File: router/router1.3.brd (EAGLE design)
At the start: 72.1 x 38.4 mm, 20 parts, among them IC1 REG1117, J1 nRF24, J4 6_PIN_SERIAL_CABLEPTH

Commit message: New router 1.3
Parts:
- S3: value FLASH -> USER
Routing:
- net GND: track 71.8 -> 69.4 mm
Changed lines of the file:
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@@
 </element>
 <element name="J4" library="SparkFun-Connectors" package="FTDI_BASIC" value="6_PIN_SERIAL_CABLEPTH" x="49.2125" y="-22.225" rot="MR0"/>
-<element name="S3" library="SparkFun-Switches" package="TACTILE_SWITCH_PTH_6.0MM" value="FLASH" x="-10.795" y="-16.8275" rot="MR270">
+<element name="S3" library="SparkFun-Switches" package="TACTILE_SWITCH_PTH_6.0MM" value="USER" x="-10.795" y="-16.8275" rot="MR270">
 <attribute name="PROD_ID" value=" SWCH-08441" x="-10.795" y="-16.8275" size="1.778" layer="28" rot="MR270" display="off"/>
 <attribute name="SF_SKU" value="COM-00097" x="-10.795" y="-16.8275" size="1.778" layer="28" rot="MR270" display="off"/>
@@
 <contactref element="C3" pad="2"/>
 <contactref element="S2" pad="3"/>
-<contactref element="S1" pad="3"/>
 <contactref element="C4" pad="2"/>
 <contactref element="C5" pad="2"/>
@@
 </polygon>
 <contactref element="J4" pad="GND"/>
-<contactref element="S3" pad="3"/>
 <contactref element="IC1" pad="1"/>
 <contactref element="J2" pad="8"/>
@@
 <wire x1="21.6281" y1="-11.1055875" x2="21.6281" y2="-3.8354" width="0.1524" layer="1"/>
 <wire x1="35.8775" y1="7.115" x2="41.5925" y2="7.115" width="0.1524" layer="1"/>
-<wire x1="-8.5344" y1="5.1562" x2="-8.5344" y2="7.59323125" width="0.1524" layer="16"/>
 <wire x1="-7.7216" y1="10.0584" x2="-6.35" y2="11.43" width="0.1524" layer="16"/>
 <wire x1="-8.5344" y1="7.59323125" x2="-7.7216" y2="8.40603125" width="0.1524" layer="16"/>
@@
 <wire x1="26.67" y1="6.0325" x2="26.67" y2="5.715" width="0.1524" layer="1"/>
 <wire x1="25.5875" y1="7.115" x2="26.67" y2="6.0325" width="0.1524" layer="1"/>
+<contactref element="S1" pad="3"/>
+<contactref element="S3" pad="3"/>
+<wire x1="-8.5344" y1="-4.0513" x2="-8.5344" y2="-13.5763" width="0" layer="19" extent="1-1"/>
+<wire x1="-8.5344" y1="5.1562" x2="-8.5344" y2="-4.0513" width="0" layer="19" extent="1-1"/>
+<wire x1="-8.5344" y1="7.59323125" x2="-8.5344" y2="5.1562" width="0" layer="19" extent="16-16"/>
 </signal>
 <signal name="RST">

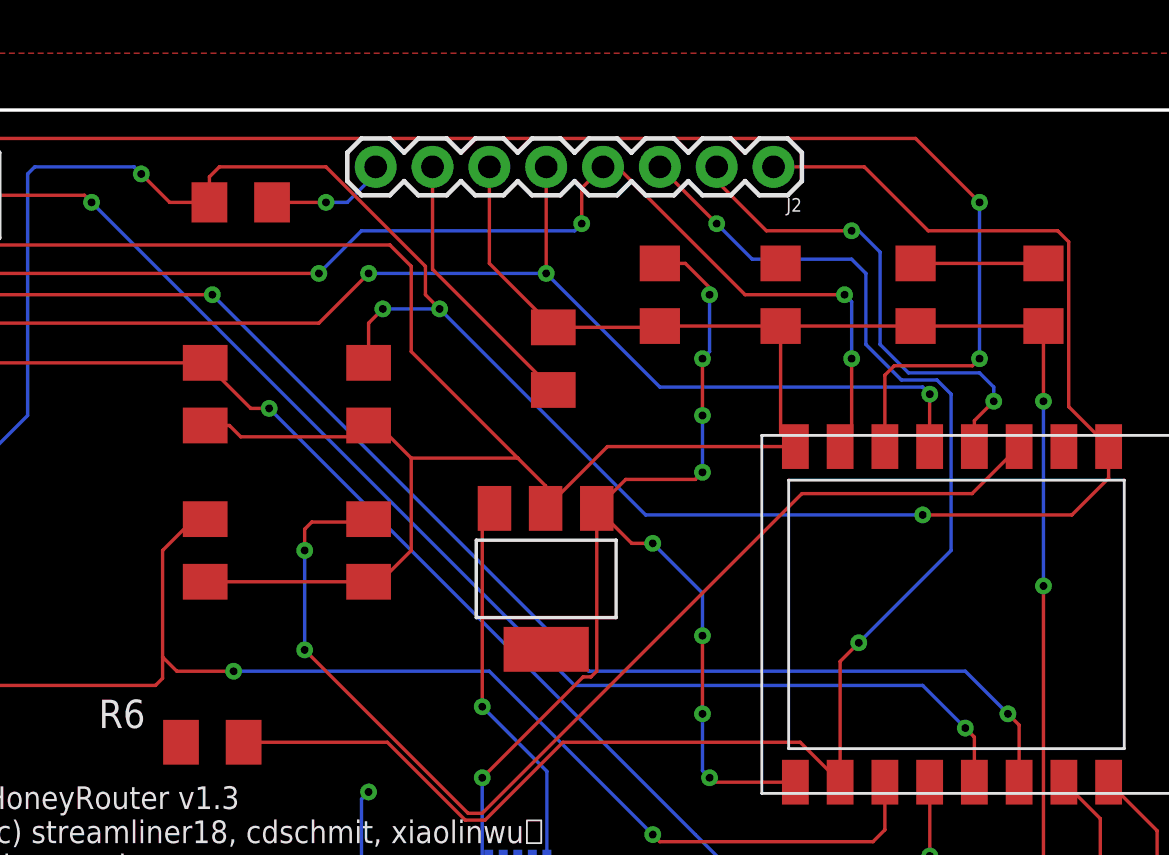
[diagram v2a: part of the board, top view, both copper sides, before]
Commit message: Post-ramp circuit fixes
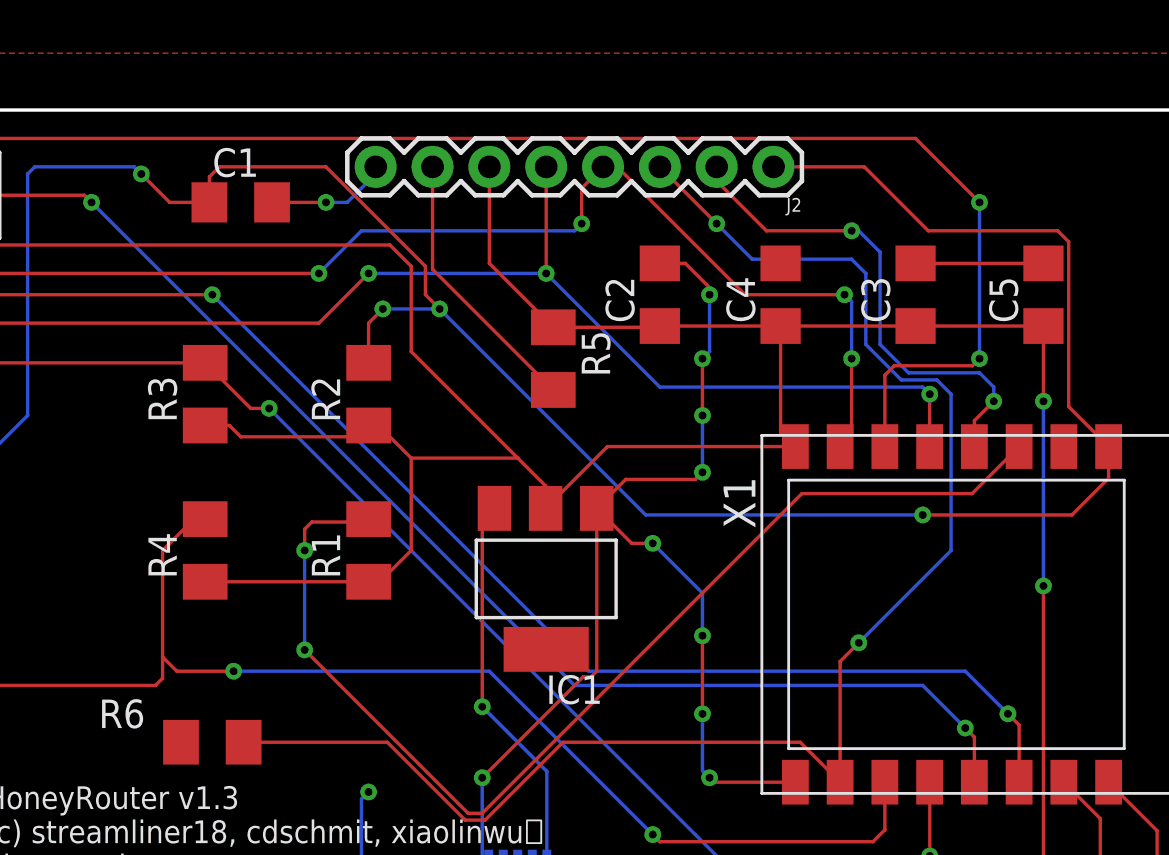
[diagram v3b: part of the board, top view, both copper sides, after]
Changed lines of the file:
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@@
 </autorouter>
 <elements>
-<element name="X1" library="adafruit" package="ESP-12" value="" x="40.005" y="-8.5725" smashed="yes" rot="R270">
-<attribute name="VALUE" x="28.005" y="-13.0725" size="1.4224" layer="27" font="vector" ratio="12" rot="R270" align="center"/>
-</element>
-<element name="R1" library="resistor" library_urn="urn:adsk.eagle:library:348" package="M1206" package3d_urn="urn:adsk.eagle:package:26088/1" value="10K" x="11.43" y="-5.715" smashed="yes" rot="R90">
-<attribute name="VALUE" x="14.2875" y="-7.3025" size="1.27" layer="27" rot="R90"/>
-</element>
-<element name="R2" library="resistor" library_urn="urn:adsk.eagle:library:348" package="M1206" package3d_urn="urn:adsk.eagle:package:26088/1" value="10K" x="11.43" y="1.27" smashed="yes" rot="R90">
-<attribute name="VALUE" x="14.2875" y="-0.3175" size="1.27" layer="27" rot="R90"/>
-</element>
-<element name="R3" library="resistor" library_urn="urn:adsk.eagle:library:348" package="M1206" package3d_urn="urn:adsk.eagle:package:26088/1" value="10K" x="4.1275" y="1.27" smashed="yes" rot="R90">
-<attribute name="VALUE" x="6.985" y="-0.3175" size="1.27" layer="27" rot="R90"/>
-</element>
-<element name="R4" library="resistor" library_urn="urn:adsk.eagle:library:348" package="M1206" package3d_urn="urn:adsk.eagle:package:26088/1" value="10K" x="4.1275" y="-5.715" smashed="yes" rot="R90">
-<attribute name="VALUE" x="6.985" y="-7.3025" size="1.27" layer="27" rot="R90"/>
-</element>
-<element name="C1" library="adafruit" package="C1206" value="100nF" x="5.715" y="9.8425" smashed="yes">
-<attribute name="VALUE" x="3.4925" y="11.2395" size="1.27" layer="27"/>
-</element>
-<element name="C2" library="adafruit" package="C1206" value="10uF" x="24.4475" y="5.715" smashed="yes" rot="R90">
-<attribute name="VALUE" x="26.8605" y="3.4925" size="1.27" layer="27" rot="R90"/>
-</element>
-<element name="C3" library="adafruit" package="C1206" value="100nF" x="35.8775" y="5.715" smashed="yes" rot="R90">
-<attribute name="VALUE" x="38.2905" y="3.4925" size="1.27" layer="27" rot="R90"/>
-</element>
+<element name="X1" library="adafruit" package="ESP-12" value="" x="40.005" y="-8.5725" rot="R270"/>
+<element name="R1" library="resistor" library_urn="urn:adsk.eagle:library:348" package="M1206" package3d_urn="urn:adsk.eagle:package:26088/1" value="10K" x="11.43" y="-5.715" rot="R90"/>
+<element name="R2" library="resistor" library_urn="urn:adsk.eagle:library:348" package="M1206" package3d_urn="urn:adsk.eagle:package:26088/1" value="10K" x="11.43" y="1.27" rot="R90"/>
+<element name="R3" library="resistor" library_urn="urn:adsk.eagle:library:348" package="M1206" package3d_urn="urn:adsk.eagle:package:26088/1" value="10K" x="4.1275" y="1.27" rot="R90"/>
+<element name="R4" library="resistor" library_urn="urn:adsk.eagle:library:348" package="M1206" package3d_urn="urn:adsk.eagle:package:26088/1" value="10K" x="4.1275" y="-5.715" rot="R90"/>
+<element name="C1" library="adafruit" package="C1206" value="100nF" x="5.715" y="9.8425"/>
+<element name="C2" library="adafruit" package="C1206" value="10uF" x="24.4475" y="5.715" rot="R90"/>
+<element name="C3" library="adafruit" package="C1206" value="100nF" x="35.8775" y="5.715" rot="R90"/>
 <element name="S1" library="SparkFun-Switches" package="TACTILE_SWITCH_PTH_6.0MM" value="FLASH" x="-10.795" y="1.905" rot="MR270">
 <attribute name="PROD_ID" value=" SWCH-08441" x="-10.795" y="1.905" size="1.778" layer="28" rot="MR270" display="off"/>
@@
 </element>
 <element name="J1" library="SparkFun-Connectors" package="2X4" value="nRF24" x="-10.16" y="10.16" rot="R180"/>
-<element name="C4" library="adafruit" package="C1206" value="10uF" x="29.845" y="5.715" smashed="yes" rot="R90">
-<attribute name="VALUE" x="32.258" y="3.4925" size="1.27" layer="27" rot="R90"/>
-</element>
-<element name="C5" library="adafruit" package="C1206" value="100nF" x="41.5925" y="5.715" smashed="yes" rot="R90">
-<attribute name="VALUE" x="44.0055" y="3.4925" size="1.27" layer="27" rot="R90"/>
-</element>
+<element name="C4" library="adafruit" package="C1206" value="10uF" x="29.845" y="5.715" rot="R90"/>
+<element name="C5" library="adafruit" package="C1206" value="100nF" x="41.5925" y="5.715" rot="R90"/>
 <element name="J2" library="SparkFun-Connectors" package="1X08" value="" x="29.5275" y="11.43" rot="R180">
 <attribute name="PROD_ID" value="CONN-08438" x="29.5275" y="11.43" size="1.778" layer="27" rot="R180" display="off"/>
 </element>
-<element name="R5" library="resistor" library_urn="urn:adsk.eagle:library:348" package="M1206" package3d_urn="urn:adsk.eagle:package:26088/1" value="220" x="19.685" y="2.8575" smashed="yes" rot="R270">
-<attribute name="VALUE" x="16.8275" y="4.445" size="1.27" layer="27" rot="R270"/>
-</element>
-<element name="J3" library="SparkFun-Connectors" package="USB-B-MICRO-SMD" value="" x="18.0975" y="-22.5425" smashed="yes" rot="MR90">
+<element name="R5" library="resistor" library_urn="urn:adsk.eagle:library:348" package="M1206" package3d_urn="urn:adsk.eagle:package:26088/1" value="220" x="19.685" y="2.8575" rot="R270"/>
+<element name="J3" library="SparkFun-Connectors" package="USB-B-MICRO-SMD" value="" x="18.0975" y="-22.5425" rot="MR90">
 <attribute name="PROD_ID" value="CONN-11752" x="18.0975" y="-22.5425" size="1.778" layer="28" rot="MR90" display="off"/>
-<attribute name="VALUE" x="13.3985" y="-23.8125" size="0.6096" layer="28" font="vector" ratio="20" rot="MR90" align="top-left"/>
 </element>
 <element name="J4" library="SparkFun-Connectors" package="FTDI_BASIC" value="6_PIN_SERIAL_CABLEPTH" x="49.2125" y="-22.225" rot="MR0"/>
@@
 <attribute name="SF_SKU" value="COM-00097" x="-10.795" y="-16.8275" size="1.778" layer="28" rot="MR270" display="off"/>
 </element>
-<element name="IC1" library="burr-brown" library_urn="urn:adsk.eagle:library:111" package="SOT223" package3d_urn="urn:adsk.eagle:package:4940/1" value="REG1117" x="19.3675" y="-6.985" smashed="yes" rot="R180">
+<element name="IC1" library="burr-brown" library_urn="urn:adsk.eagle:library:111" package="SOT223" package3d_urn="urn:adsk.eagle:package:4940/1" value="REG1117" x="19.3675" y="-6.985" rot="R180">
 <attribute name="MF" value="" x="19.3675" y="-6.985" size="1.778" layer="27" rot="R180" display="off"/>
 <attribute name="MPN" value="REG1117" x="19.3675" y="-6.985" size="1.778" layer="27" rot="R180" display="off"/>
 <attribute name="OC_FARNELL" value="1097566" x="19.3675" y="-6.985" size="1.778" layer="27" rot="R180" display="off"/>
 <attribute name="OC_NEWARK" value="14P6981" x="19.3675" y="-6.985" size="1.778" layer="27" rot="R180" display="off"/>
-<attribute name="VALUE" x="22.1615" y="-1.143" size="1.27" layer="27" ratio="10" rot="R180"/>
 </element>
 <element name="R6" library="resistor" library_urn="urn:adsk.eagle:library:348" package="M1206" package3d_urn="urn:adsk.eagle:package:26088/1" value="10K" x="4.445" y="-14.2875" smashed="yes">
